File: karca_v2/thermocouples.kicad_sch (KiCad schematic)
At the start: 11 parts, among them J8 Screw_Terminal_01x08, U14 NUP4202, U15 NUP4202, U16 NUP4202, U17 TLV9304xD

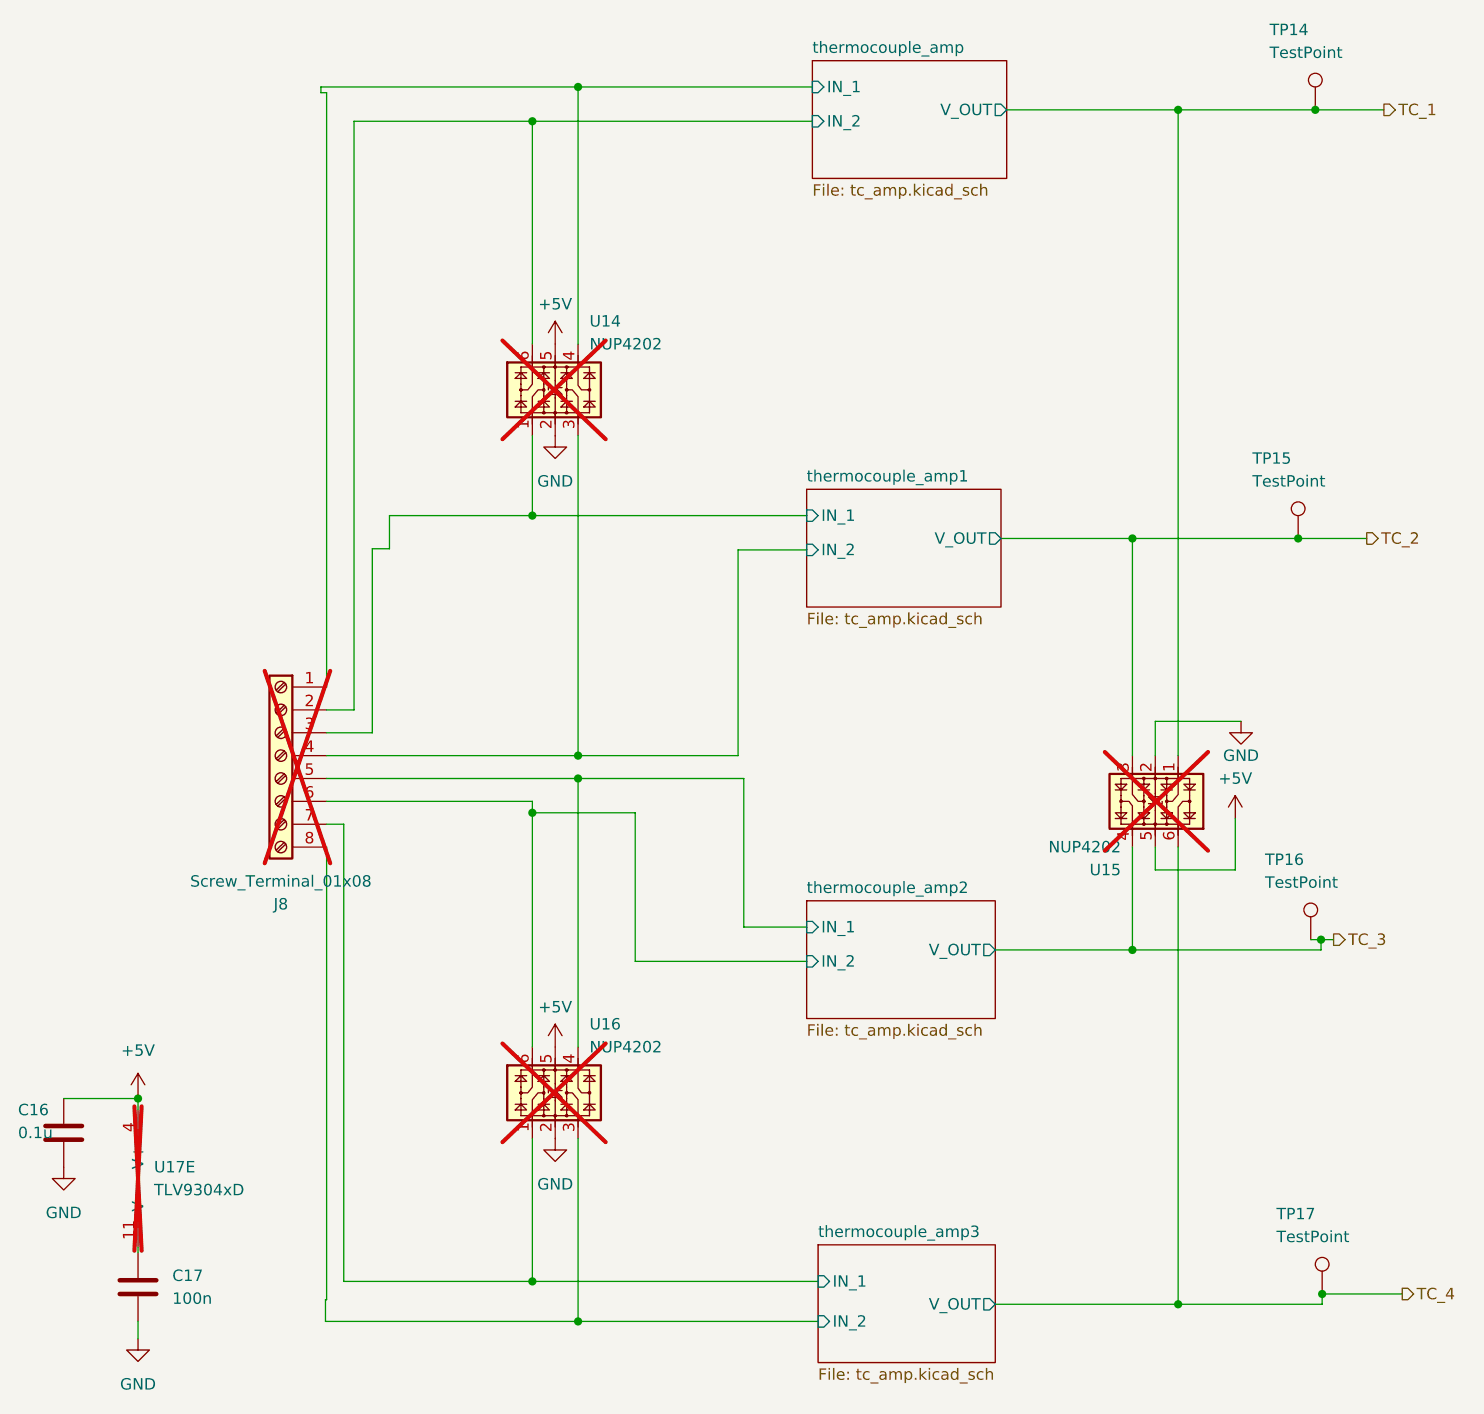
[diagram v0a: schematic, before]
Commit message: new design: chip on board
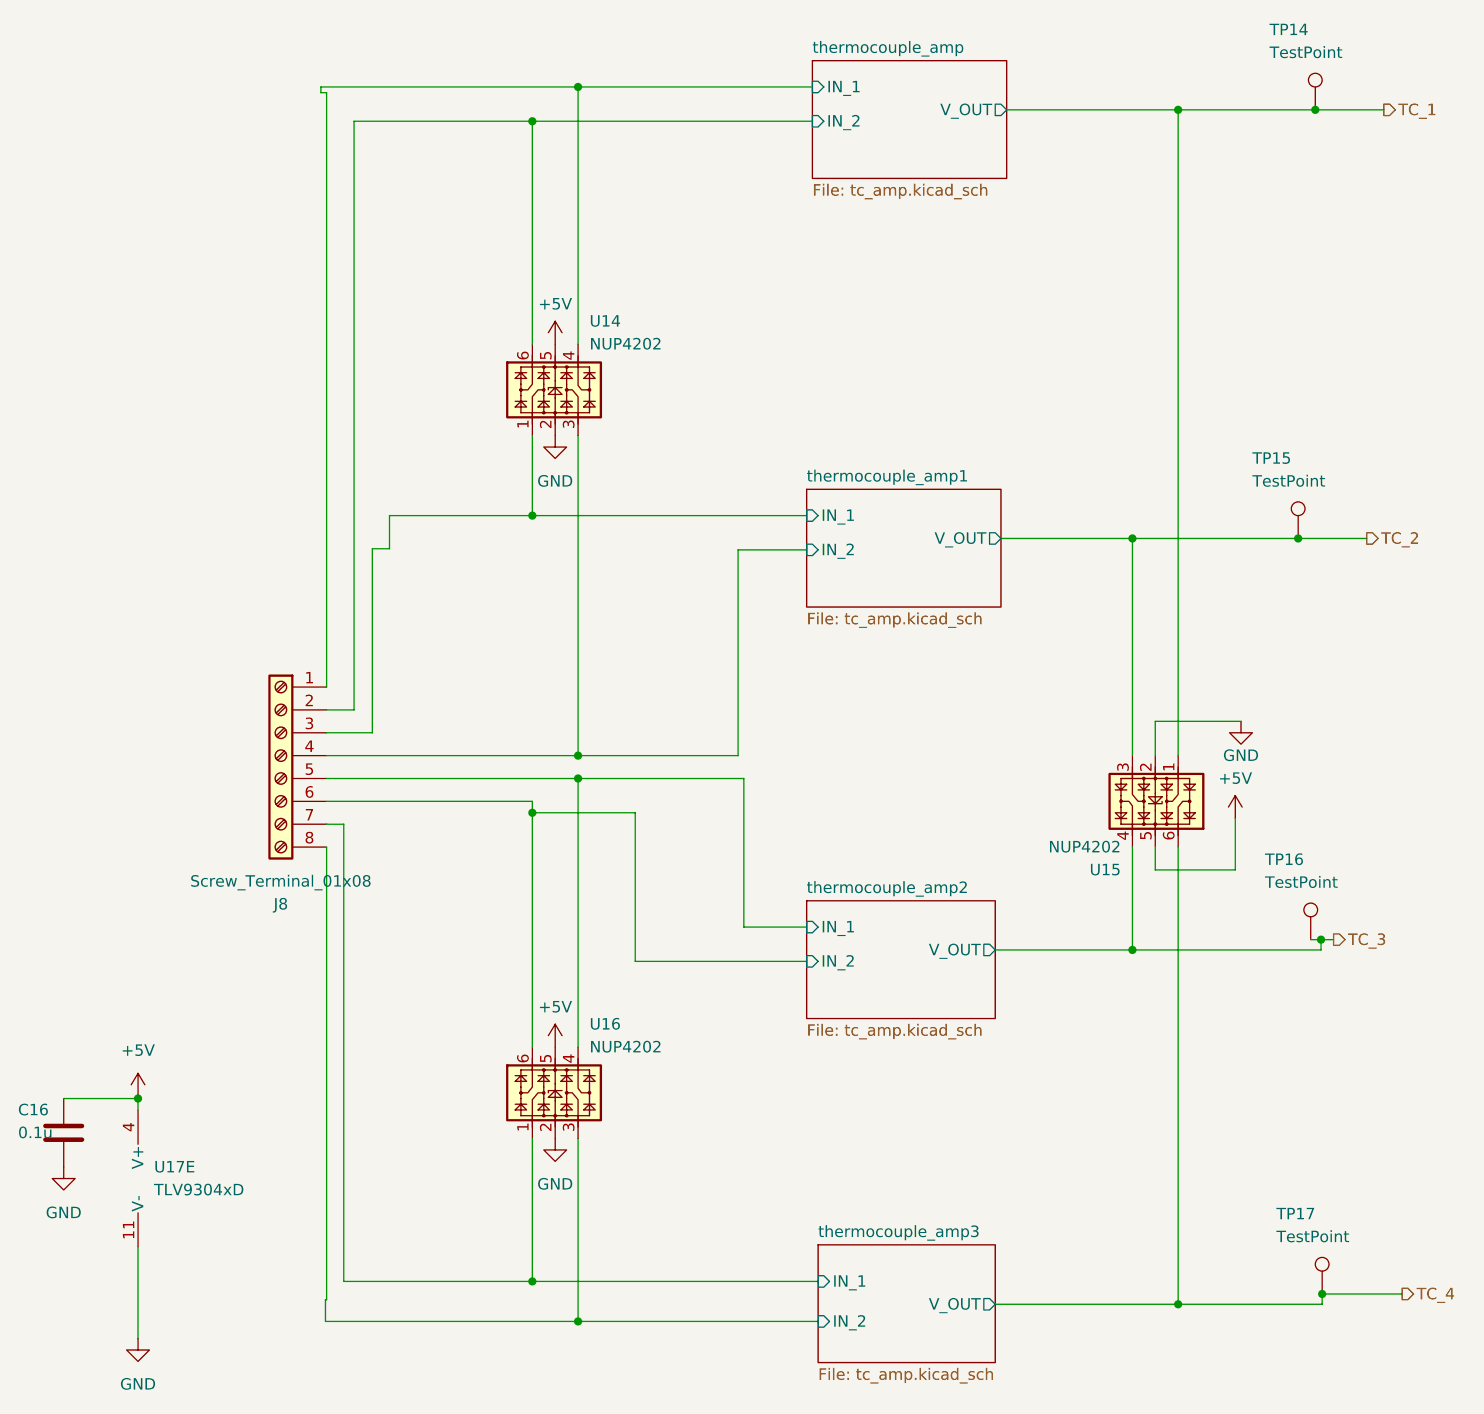
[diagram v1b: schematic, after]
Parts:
- removed C17: 100n, Capacitor_SMD:C_1206_3216Metric, symbol Device:C
- J8, U14, U15, U16, U17: now fitted
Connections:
- net GND: now also U17.11 (V-)
